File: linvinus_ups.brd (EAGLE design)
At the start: 34 x 36.8 mm, 24 parts, among them J1 BATTERY_CONNDEANS, Q1 IRF7240PBF, Q2 IRF7240PBF, Q3 BSS123, Q4 IRF7240PBF

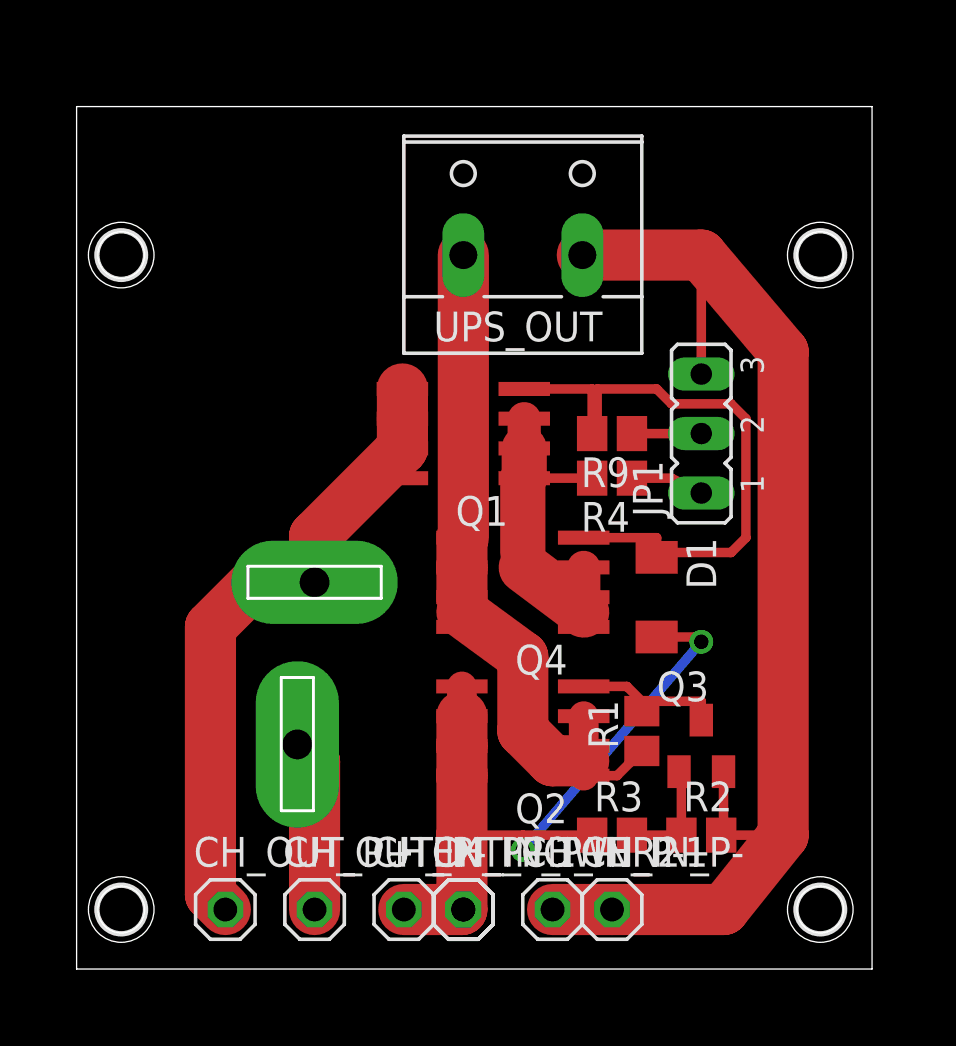
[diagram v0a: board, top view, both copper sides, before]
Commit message: fix, completely close Q4 if vbatt > external power
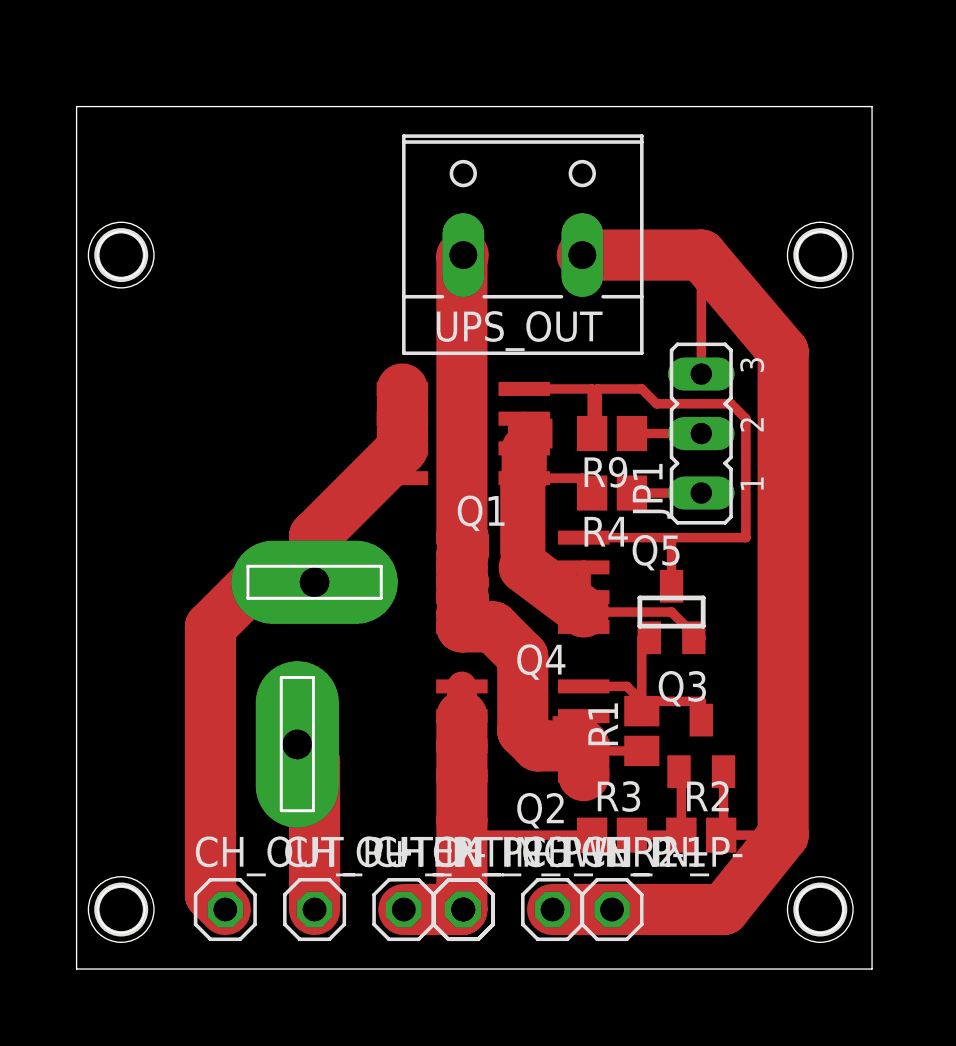
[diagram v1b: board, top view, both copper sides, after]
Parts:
- removed D1: (no value), semicon-smd-ipc:SOD80
- added Q5: FDN360P, transistor-power:SUPER-SOT3
- moved R4 0.63 mm to (29.2, 35.6)
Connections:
- net EXT_POWER2+: no longer D1.2
- net N$1: now also Q5.1
- net N$10: now also Q5.3; no longer D1.1
- net N$5: now also Q5.2
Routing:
- net EXT_POWER2+: track 31.9 -> 17.8 mm, vias 2 -> 0
- net N$5: track 15.0 -> 21.0 mm
- net N$1: track 6.51 -> 9.64 mm
- net BAT+: track 27.4 -> 28.6 mm
- net N$10: track 26.8 -> 27.7 mm
- net N$6: track 30.9 -> 30.4 mm

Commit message: fix v2, completely close Q4 if vbatt > external power
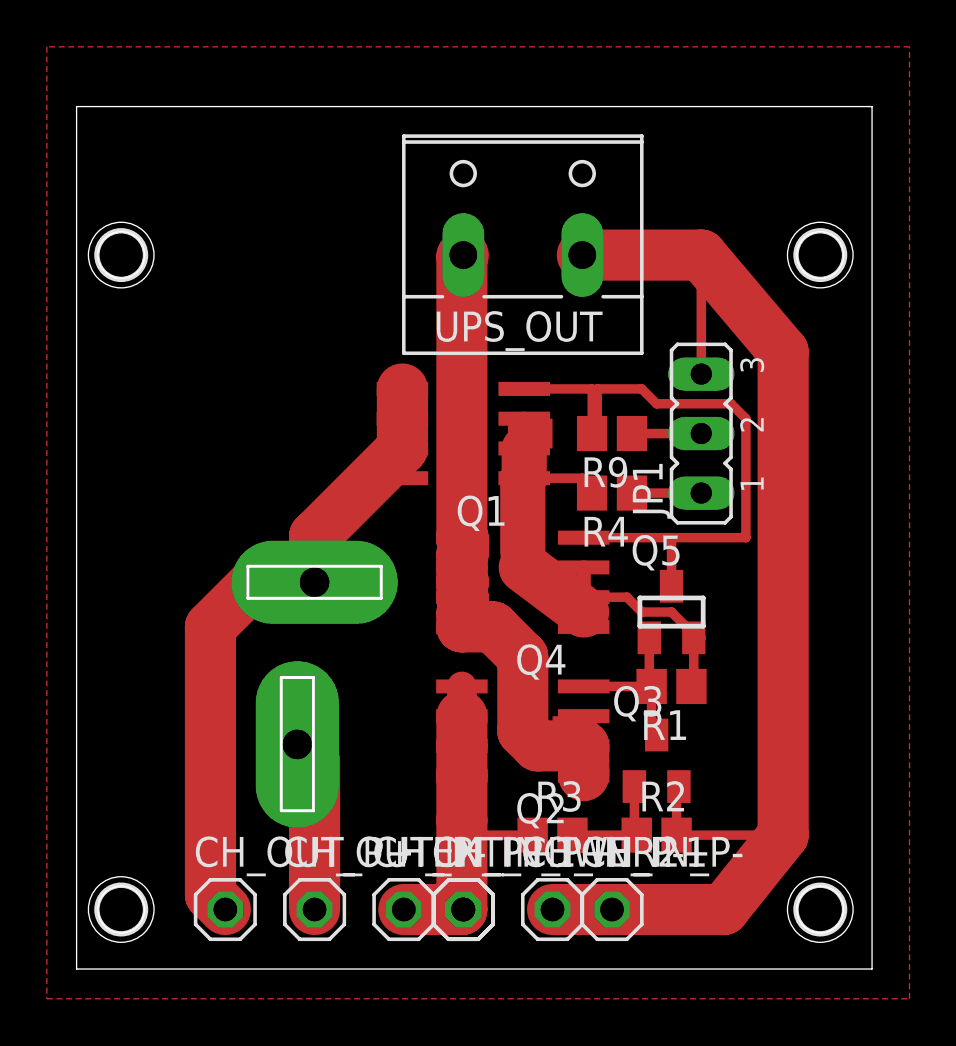
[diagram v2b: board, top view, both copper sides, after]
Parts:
- Q5: value FDN360P -> irlml6402
- R1: value 100k -> 10k
- R2: value 30k -> 22k
- moved R3 2.54 mm to (26.7, 21.0)
- moved R1 2.29 mm to (31.8, 27.3), turned to 180 degrees
- moved Q3 2.01 mm to (31.1, 24.1)
- moved R2 1.91 mm to (31.1, 21.0)
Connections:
- net N$5: now also R1.1
- net N$6: no longer R1.1
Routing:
- net EXT_POWER2+: track 17.8 -> 15.3 mm
- net N$1: track 9.64 -> 7.18 mm
- net N$5: track 21.0 -> 23.4 mm
- net N$6: track 30.4 -> 28.3 mm
- net GND: track 53.0 -> 54.2 mm
- added copper zone on layer 1, net GND
